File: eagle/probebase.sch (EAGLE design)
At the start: 11 parts, among them M1 TPTP14R, M2 TPTP14R, M3 TPTP14R, P1- TPTP14R, P2- TPTP14R, P3- TPTP14R, P4- TPTP14R

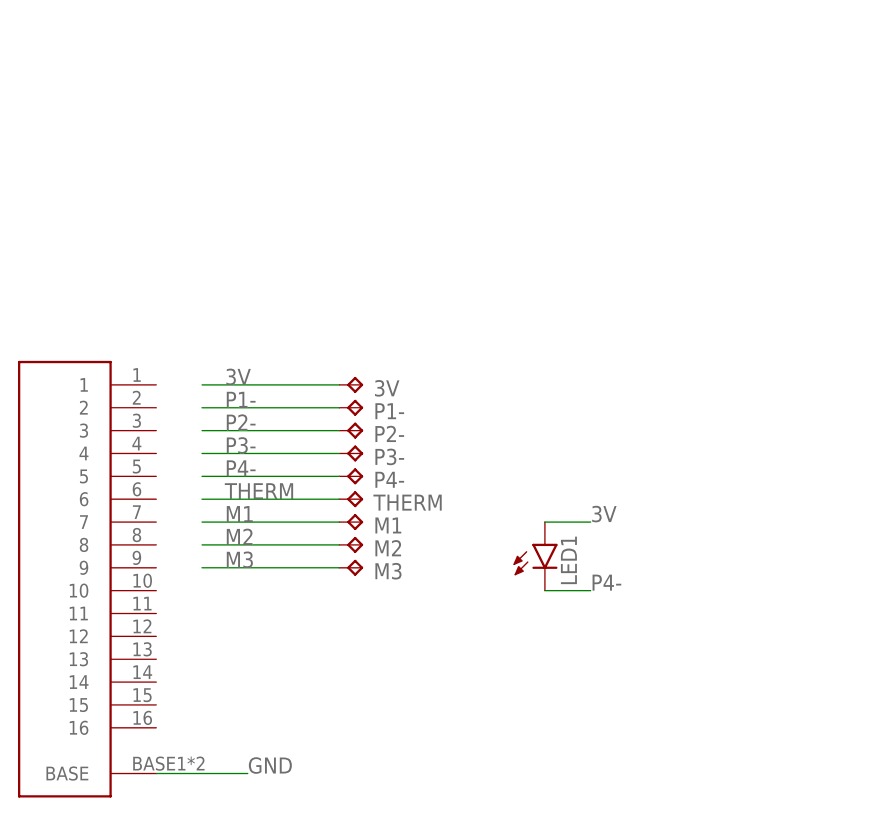
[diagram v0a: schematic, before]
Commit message: decided on ffc wire layout.
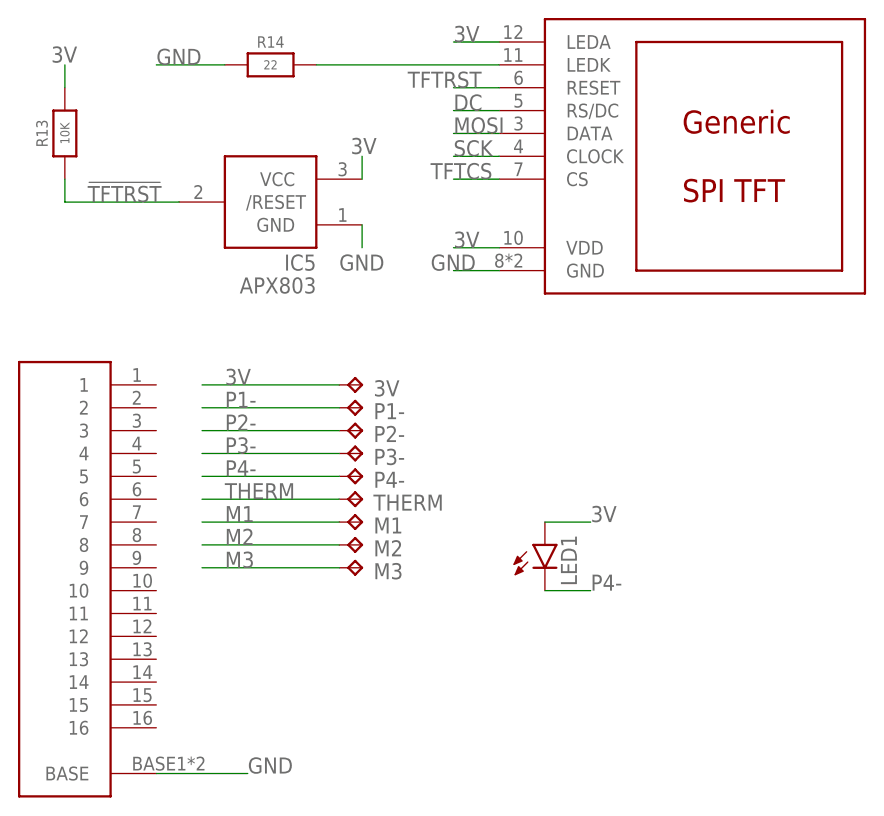
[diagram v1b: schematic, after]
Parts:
- added IC5: APX803, adafruit:AXP083-SAG
- added R13: 10K, microbuilder:RESISTOR_0603_NOOUT
- added R14: 22, microbuilder:RESISTOR_0603_NOOUT
- added U$4: TFT, general:TFT
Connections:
- new net !TFTRST: IC5./RESET, R13.1
- new net DC: U$4.RS/DC
- new net MOSI: U$4.DATA
- new net N$1: R14.2, U$4.LEDK
- new net SCK: U$4.CLOCK
- new net TFTCS: U$4.CS
- new net TFTRST: U$4.RESET
- net 3V: now also IC5.VCC, R13.2, U$4.LEDA, U$4.VDD
- net GND: now also IC5.GND, R14.1, U$4.GND
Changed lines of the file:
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@@
 <setting verticaltext="up"/>
 </settings>
-<grid distance="0.1" unitdist="inch" unit="inch" style="dots" multiple="1" display="no" altdistance="0.01" altunitdist="inch" altunit="inch"/>
+<grid distance="0.1" unitdist="inch" unit="inch" style="lines" multiple="1" display="no" altdistance="0.01" altunitdist="inch" altunit="inch"/>
 <layers>
 <layer number="1" name="Top" color="4" fill="1" visible="no" active="no"/>
@@
 </variantdefs>
 <classes>
-<class number="0" name="default" width="0" drill="0">
+<class number="0" name="default" width="0.1524" drill="0">
+<clearance class="0" value="0.1524"/>
+</class>
+<class number="1" name="battery" width="0.3048" drill="0">
+<clearance class="1" value="0.1524"/>
 </class>
 </classes>
@@
 <part name="M2" library="testpad" library_urn="urn:adsk.eagle:library:385" deviceset="TP" device="TP14R" package3d_urn="urn:adsk.eagle:package:27966/1"/>
 <part name="M3" library="testpad" library_urn="urn:adsk.eagle:library:385" deviceset="TP" device="TP14R" package3d_urn="urn:adsk.eagle:package:27966/1"/>
+<part name="IC5" library="adafruit" deviceset="AXP083" device="-SAG" value="APX803"/>
+<part name="R13" library="microbuilder" deviceset="RESISTOR" device="_0603_NOOUT" value="10K"/>
+<part name="R14" library="microbuilder" deviceset="RESISTOR" device="_0603_NOOUT" value="22"/>
+<part name="U$4" library="general" deviceset="TFT" device=""/>
 </parts>
 <sheets>
@@
 <attribute name="TP_SIGNAL_NAME" x="36.83" y="24.13" size="1.778" layer="97" rot="R270"/>
 </instance>
+<instance part="IC5" gate="G$1" x="27.94" y="66.04" smashed="yes" rot="MR0">
+<attribute name="NAME" x="33.02" y="58.42" size="1.778" layer="95" rot="MR0"/>
+<attribute name="VALUE" x="33.02" y="55.88" size="1.778" layer="96" rot="MR0"/>
+</instance>
+<instance part="R13" gate="G$1" x="5.08" y="73.66" smashed="yes" rot="R90">
+<attribute name="NAME" x="2.54" y="73.66" size="1.27" layer="95" font="vector" rot="R90" align="center"/>
+<attribute name="VALUE" x="5.08" y="73.66" size="1.016" layer="96" font="vector" ratio="15" rot="R90" align="center"/>
+</instance>
+<instance part="R14" gate="G$1" x="27.94" y="81.28" smashed="yes">
+<attribute name="NAME" x="27.94" y="83.82" size="1.27" layer="95" font="vector" align="center"/>
+<attribute name="VALUE" x="27.94" y="81.28" size="1.016" layer="96" font="vector" ratio="15" align="center"/>
+</instance>
+<instance part="U$4" gate="G$1" x="78.74" y="71.12" smashed="yes"/>
 </instances>
 <busses>
@@
 <label x="63.5" y="30.48" size="1.778" layer="95"/>
 </segment>
+<segment>
+<pinref part="R13" gate="G$1" pin="2"/>
+<wire x1="5.08" y1="78.74" x2="5.08" y2="81.28" width="0.1524" layer="91"/>
+<label x="3.556" y="81.534" size="1.778" layer="95"/>
+</segment>
+<segment>
+<wire x1="38.1" y1="68.58" x2="38.1" y2="71.12" width="0.1524" layer="91"/>
+<pinref part="IC5" gate="G$1" pin="VCC"/>
+<label x="36.83" y="71.374" size="1.778" layer="95"/>
+</segment>
+<segment>
+<pinref part="U$4" gate="G$1" pin="LEDA"/>
+<wire x1="53.34" y1="83.82" x2="48.26" y2="83.82" width="0.1524" layer="91"/>
+<label x="48.26" y="83.82" size="1.778" layer="95"/>
+</segment>
+<segment>
+<pinref part="U$4" gate="G$1" pin="VDD"/>
+<wire x1="53.34" y1="60.96" x2="48.26" y2="60.96" width="0.1524" layer="91"/>
+<label x="48.26" y="60.96" size="1.778" layer="95"/>
+</segment>
 </net>
 <net name="P1-" class="0">
@@
 <label x="25.4" y="2.54" size="1.778" layer="95"/>
 </segment>
+<segment>
+<pinref part="R14" gate="G$1" pin="1"/>
+<wire x1="22.86" y1="81.28" x2="15.24" y2="81.28" width="0.1524" layer="91"/>
+<label x="15.24" y="81.28" size="1.778" layer="95"/>
+</segment>
+<segment>
+<wire x1="38.1" y1="63.5" x2="38.1" y2="60.96" width="0.1524" layer="91"/>
+<pinref part="IC5" gate="G$1" pin="GND"/>
+<label x="35.56" y="58.42" size="1.778" layer="95"/>
+</segment>
+<segment>
+<pinref part="U$4" gate="G$1" pin="GND"/>
+<wire x1="53.34" y1="58.42" x2="48.26" y2="58.42" width="0.1524" layer="91"/>
+<label x="45.72" y="58.42" size="1.778" layer="95"/>
+</segment>
 </net>
 <net name="M3" class="0">
@@
 </segment>
 </net>
+<net name="TFTCS" class="0">
+<segment>
+<pinref part="U$4" gate="G$1" pin="CS"/>
+<wire x1="53.34" y1="68.58" x2="48.26" y2="68.58" width="0.1524" layer="91"/>
+<label x="45.72" y="68.58" size="1.778" layer="95"/>
+</segment>
+</net>
+<net name="TFTRST" class="0">
+<segment>
+<pinref part="U$4" gate="G$1" pin="RESET"/>
+<wire x1="53.34" y1="78.74" x2="48.26" y2="78.74" width="0.1524" layer="91"/>
+<label x="43.18" y="78.74" size="1.778" layer="95"/>
+</segment>
+</net>
+<net name="DC" class="0">
+<segment>
+<pinref part="U$4" gate="G$1" pin="RS/DC"/>
+<wire x1="53.34" y1="76.2" x2="48.26" y2="76.2" width="0.1524" layer="91"/>
+<label x="48.26" y="76.2" size="1.778" layer="95"/>
+</segment>
+</net>
+<net name="SCK" class="0">
+<segment>
+<pinref part="U$4" gate="G$1" pin="CLOCK"/>
+<wire x1="53.34" y1="71.12" x2="48.26" y2="71.12" width="0.1524" layer="91"/>
+<label x="48.26" y="71.12" size="1.778" layer="95"/>
+</segment>
+</net>
+<net name="MOSI" class="0">
+<segment>
+<pinref part="U$4" gate="G$1" pin="DATA"/>
+<wire x1="53.34" y1="73.66" x2="48.26" y2="73.66" width="0.1524" layer="91"/>
+<label x="48.26" y="73.66" size="1.778" layer="95"/>
+</segment>
+</net>
+<net name="!TFTRST" class="0">
+<segment>
+<pinref part="IC5" gate="G$1" pin="/RESET"/>
+<label x="7.62" y="66.04" size="1.778" layer="95"/>
+<pinref part="R13" gate="G$1" pin="1"/>
+<wire x1="17.78" y1="66.04" x2="5.08" y2="66.04" width="0.1524" layer="91"/>
+<wire x1="5.08" y1="66.04" x2="5.08" y2="68.58" width="0.1524" layer="91"/>
+</segment>
+</net>
+<net name="N$1" class="0">
+<segment>
+<pinref part="R14" gate="G$1" pin="2"/>
+<pinref part="U$4" gate="G$1" pin="LEDK"/>
+<wire x1="33.02" y1="81.28" x2="53.34" y2="81.28" width="0.1524" layer="91"/>
+</segment>
+</net>

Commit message: First order of probe, probebase and FFC breakout PCBs for 22mm enclosure
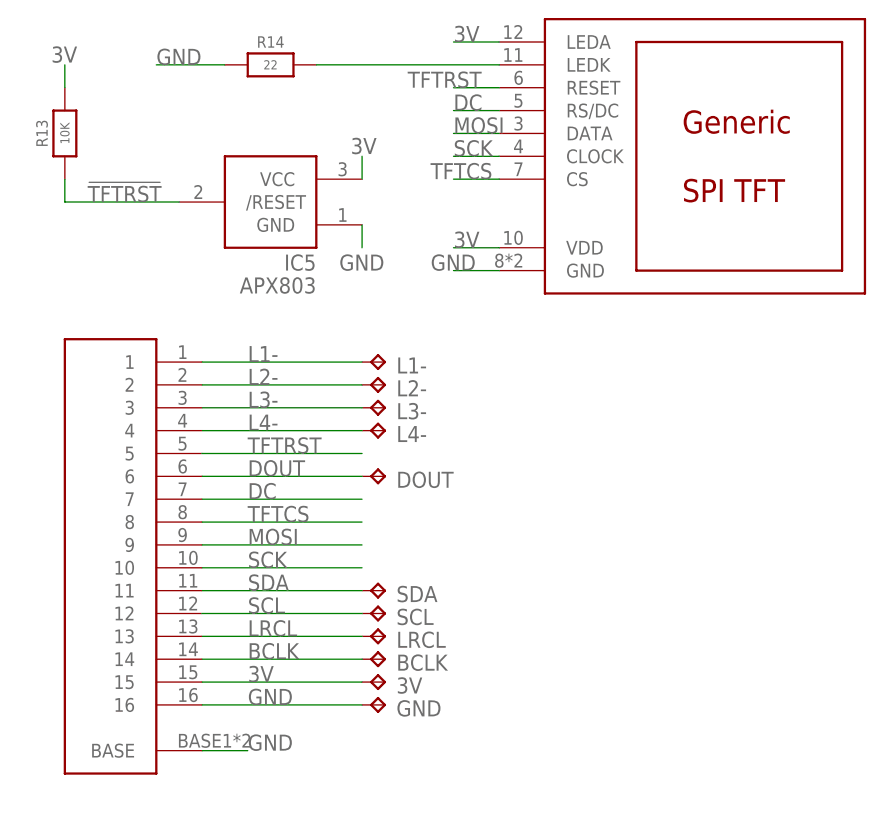
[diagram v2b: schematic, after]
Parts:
- removed LED1: (no value), led:LED3MM
- removed M1, M2, M3, P1-, P2-, P3-, P4-, THERM: TPTP14R, testpad:TPTP14R
- removed U$1: 16PINFFC, general:16PINFFC
- added BCLK, DOUT, GND, L1-, L2-, L3-, L4-, LRCL, SCL, SDA: TPTP14R, testpad:TPTP14R
- added U$3: 16PINFFC, general:16PINFFC
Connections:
- removed net M1: M1.TP
- removed net M2: M2.TP
- removed net M3: M3.TP
- removed net P1-: P1-.TP
- removed net P2-: P2-.TP
- removed net P3-: P3-.TP
- removed net P4-: LED1.C, P4-.TP
- removed net THERM: THERM.TP
- new net BCLK: BCLK.TP, U$3.14
- new net DOUT: DOUT.TP, U$3.6
- new net L1-: L1-.TP, U$3.1
- new net L2-: L2-.TP, U$3.2
- new net L3-: L3-.TP, U$3.3
- new net L4-: L4-.TP, U$3.4
- new net LRCL: LRCL.TP, U$3.13
- new net SCL: SCL.TP, U$3.12
- new net SDA: SDA.TP, U$3.11
- net 3V: now also U$3.15; no longer LED1.A
- net DC: now also U$3.7
- net GND: now also GND.TP, U$3.16, U$3.BASE; no longer U$1.BASE
- net MOSI: now also U$3.9
- net SCK: now also U$3.10
- net TFTCS: now also U$3.8
- net TFTRST: now also U$3.5
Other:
- moved on the sheet: 3V

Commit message: Redesigned probe base pcb
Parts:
- added BTN: TPTP14R, testpad:TPTP14R
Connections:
- new net BTN: BTN.TP, U$3.16
- net GND: no longer U$3.16
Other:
- moved on the sheet: GND
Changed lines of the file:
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@@
 <clearance class="0" value="0.1524"/>
 </class>
-<class number="1" name="battery" width="0.3048" drill="0">
+<class number="1" name="battery" width="0.254" drill="0">
 <clearance class="1" value="0.1524"/>
 </class>
@@
 <part name="SCL" library="testpad" library_urn="urn:adsk.eagle:library:385" deviceset="TP" device="TP14R" package3d_urn="urn:adsk.eagle:package:27966/1"/>
 <part name="3V" library="testpad" library_urn="urn:adsk.eagle:library:385" deviceset="TP" device="TP14R" package3d_urn="urn:adsk.eagle:package:27966/1"/>
-<part name="GND" library="testpad" library_urn="urn:adsk.eagle:library:385" deviceset="TP" device="TP14R" package3d_urn="urn:adsk.eagle:package:27966/1"/>
+<part name="BTN" library="testpad" library_urn="urn:adsk.eagle:library:385" deviceset="TP" device="TP14R" package3d_urn="urn:adsk.eagle:package:27966/1"/>
 <part name="LRCL" library="testpad" library_urn="urn:adsk.eagle:library:385" deviceset="TP" device="TP14R" package3d_urn="urn:adsk.eagle:package:27966/1"/>
 <part name="BCLK" library="testpad" library_urn="urn:adsk.eagle:library:385" deviceset="TP" device="TP14R" package3d_urn="urn:adsk.eagle:package:27966/1"/>
+<part name="GND" library="testpad" library_urn="urn:adsk.eagle:library:385" deviceset="TP" device="TP14R" package3d_urn="urn:adsk.eagle:package:27966/1"/>
 </parts>
 <sheets>
@@
 <attribute name="TP_SIGNAL_NAME" x="39.37" y="11.43" size="1.778" layer="97" rot="R270"/>
 </instance>
-<instance part="GND" gate="G$1" x="40.64" y="10.16" smashed="yes" rot="R270">
+<instance part="BTN" gate="G$1" x="40.64" y="10.16" smashed="yes" rot="R270">
 <attribute name="NAME" x="41.91" y="8.89" size="1.778" layer="95"/>
 <attribute name="TP_SIGNAL_NAME" x="39.37" y="8.89" size="1.778" layer="97" rot="R270"/>
@@
 <attribute name="NAME" x="41.91" y="13.97" size="1.778" layer="95"/>
 <attribute name="TP_SIGNAL_NAME" x="39.37" y="13.97" size="1.778" layer="97" rot="R270"/>
+</instance>
+<instance part="GND" gate="G$1" x="63.5" y="45.72" smashed="yes" rot="R270">
+<attribute name="NAME" x="64.77" y="44.45" size="1.778" layer="95"/>
+<attribute name="TP_SIGNAL_NAME" x="62.23" y="44.45" size="1.778" layer="97" rot="R270"/>
 </instance>
 </instances>
@@
 </busses>
 <nets>
-<net name="3V" class="0">
+<net name="3V" class="1">
 <segment>
 <pinref part="R13" gate="G$1" pin="2"/>
@@
 </segment>
 </net>
-<net name="GND" class="0">
+<net name="GND" class="1">
 <segment>
 <pinref part="R14" gate="G$1" pin="1"/>
@@
 </segment>
 <segment>
-<pinref part="U$3" gate="G$1" pin="16"/>
 <pinref part="GND" gate="G$1" pin="TP"/>
-<wire x1="20.32" y1="10.16" x2="38.1" y2="10.16" width="0.1524" layer="91"/>
-<label x="25.4" y="10.16" size="1.778" layer="95"/>
+<wire x1="60.96" y1="45.72" x2="53.34" y2="45.72" width="0.1524" layer="91"/>
+<label x="53.34" y="45.72" size="1.778" layer="95"/>
 </segment>
 </net>
@@
 </segment>
 </net>
+<net name="BTN" class="0">
+<segment>
+<pinref part="U$3" gate="G$1" pin="16"/>
+<pinref part="BTN" gate="G$1" pin="TP"/>
+<wire x1="20.32" y1="10.16" x2="38.1" y2="10.16" width="0.1524" layer="91"/>
+<label x="25.4" y="10.16" size="1.778" layer="95"/>
+</segment>
+</net>
